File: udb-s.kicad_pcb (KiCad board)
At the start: 2 copper layers, 16.4 x 15.7 mm, 9 parts, among them J1 TYPE-C-31-M-12, J2 Conn_01x04, J3 Conn_01x04, U1 TPD4E05U06DQAR

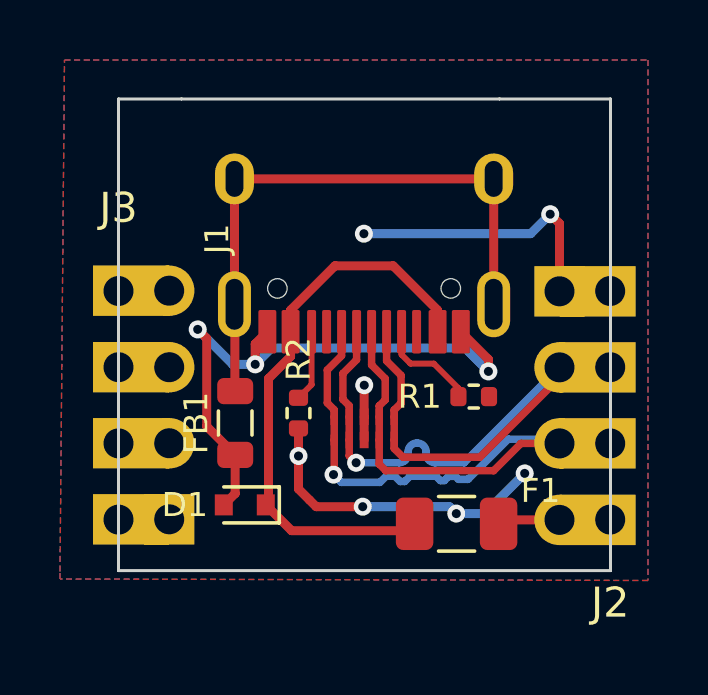
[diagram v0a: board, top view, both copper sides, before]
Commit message: Fuse footprint update.
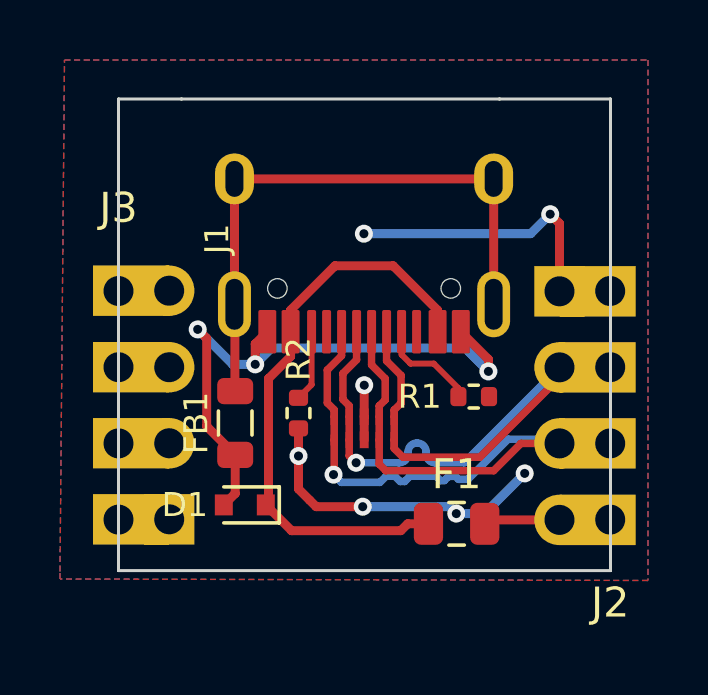
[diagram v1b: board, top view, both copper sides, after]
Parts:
- F1: footprint Fuse:Fuse_1206_3216Metric -> Fuse:Fuse_0805_2012Metric
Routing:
- net 5V: track 1.95 -> 2.55 mm
